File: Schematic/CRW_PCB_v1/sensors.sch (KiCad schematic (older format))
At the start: 17 parts

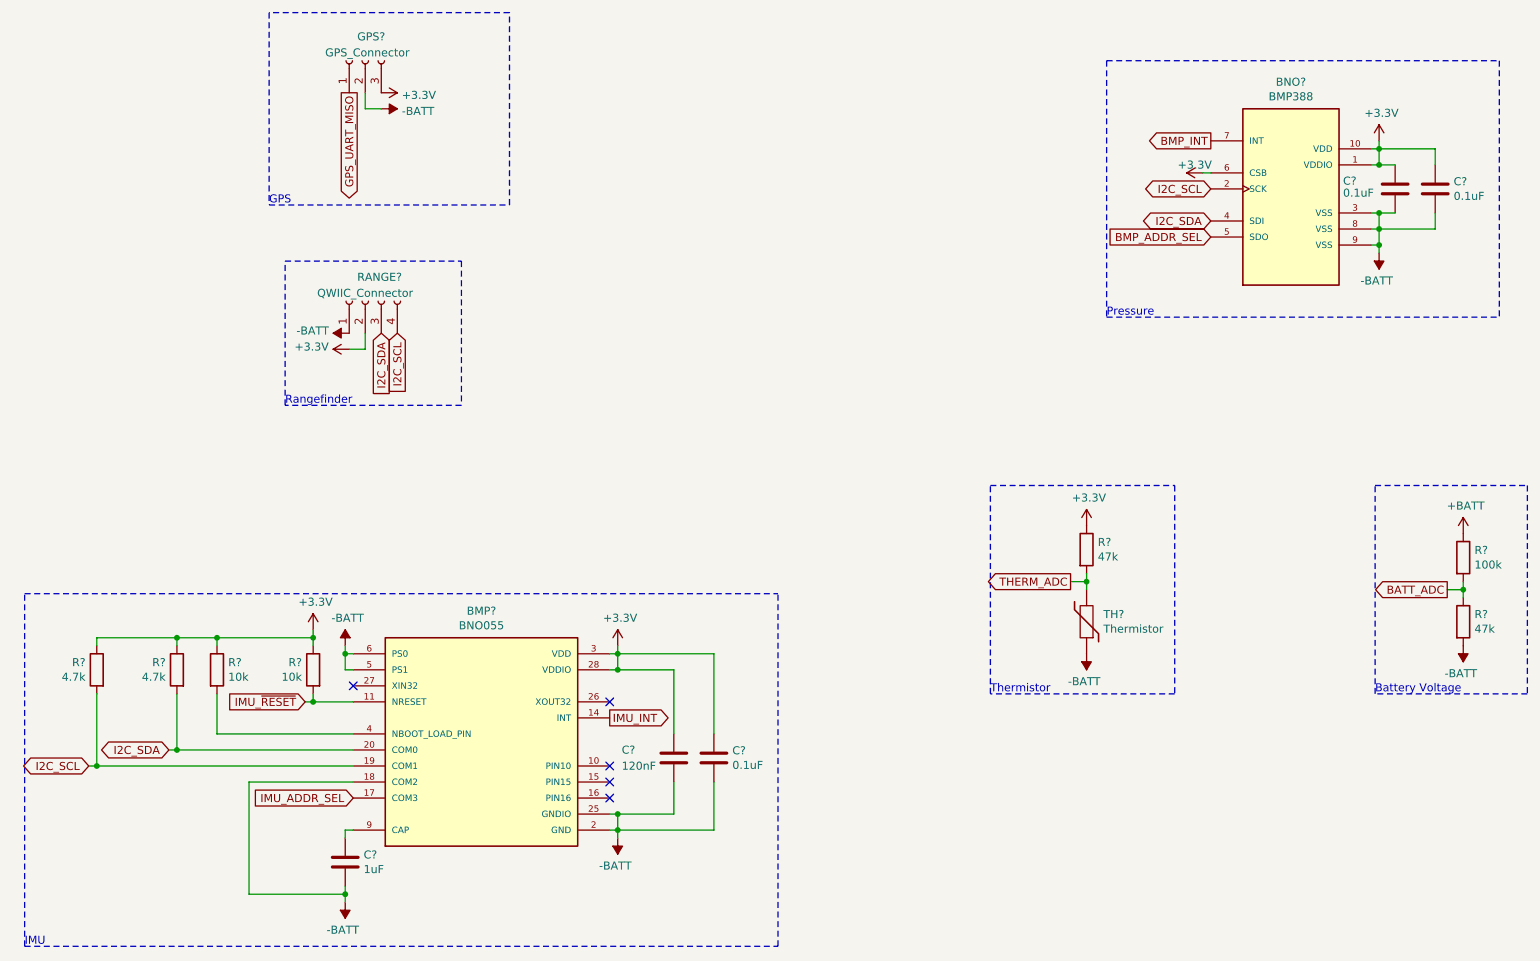
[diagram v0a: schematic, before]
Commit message: Added Hotwire Connection
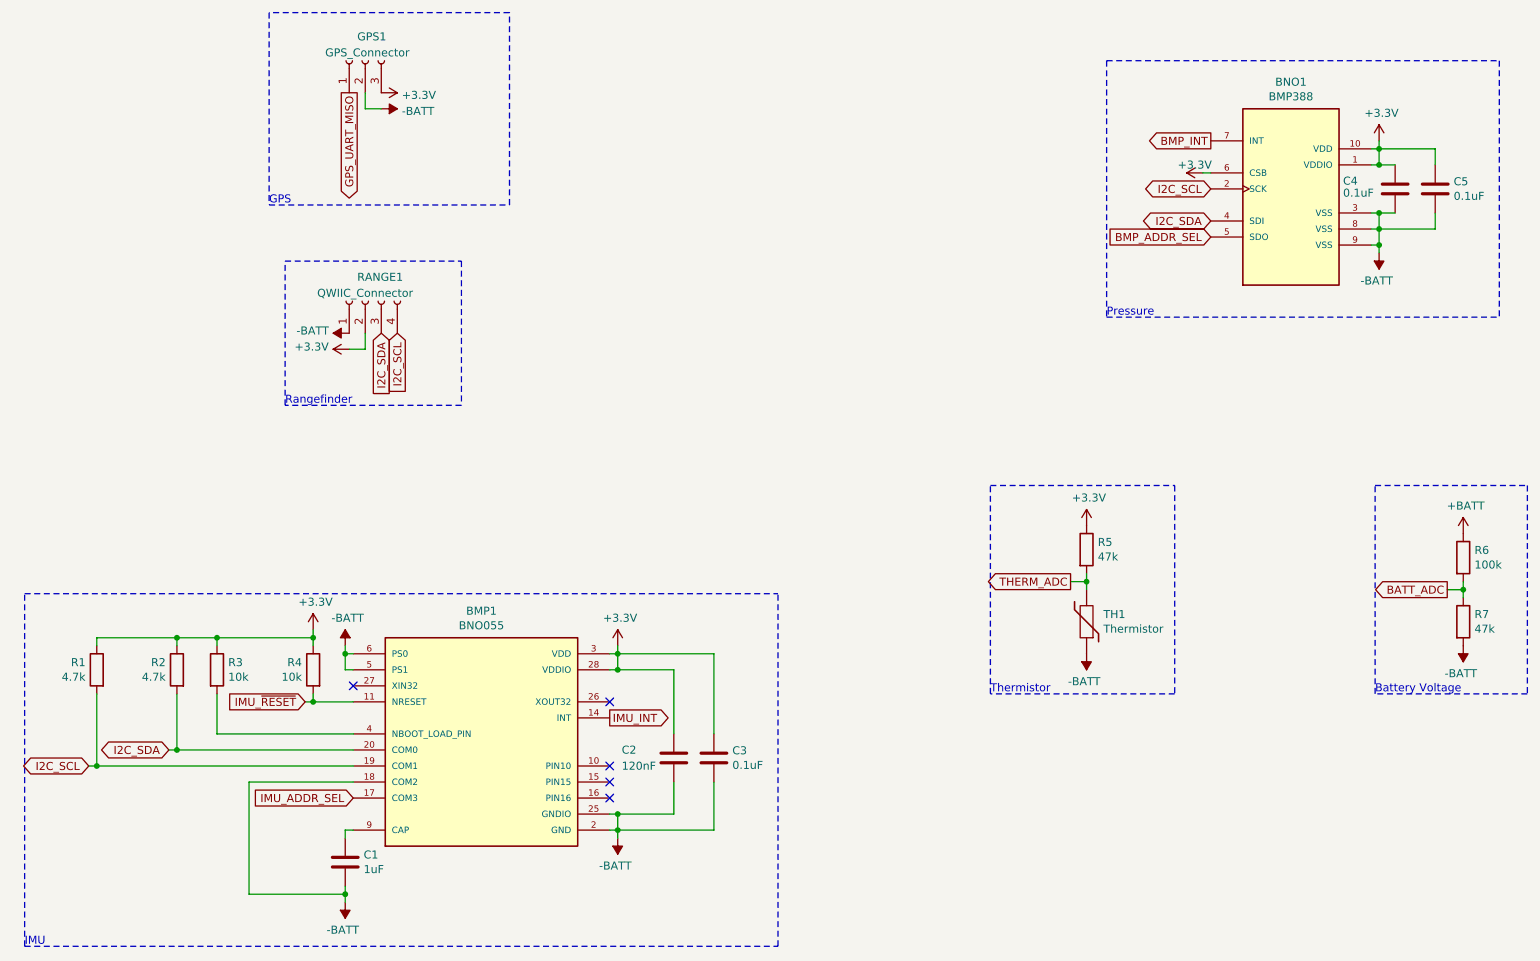
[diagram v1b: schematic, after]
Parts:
- gave numbers to parts that had none: 17
